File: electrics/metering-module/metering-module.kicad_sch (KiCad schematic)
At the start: 39 parts, among them J1 North, J2 South, J3 West, J4 East, Q1 MMBT3904, Q2 MMBT3904, U1 LTV-817S, U2 LTV-817S, U3 BA033CC0FP-E2, U4 MAX3486, U5 MAX3486, U6 MCP23009-E_SS

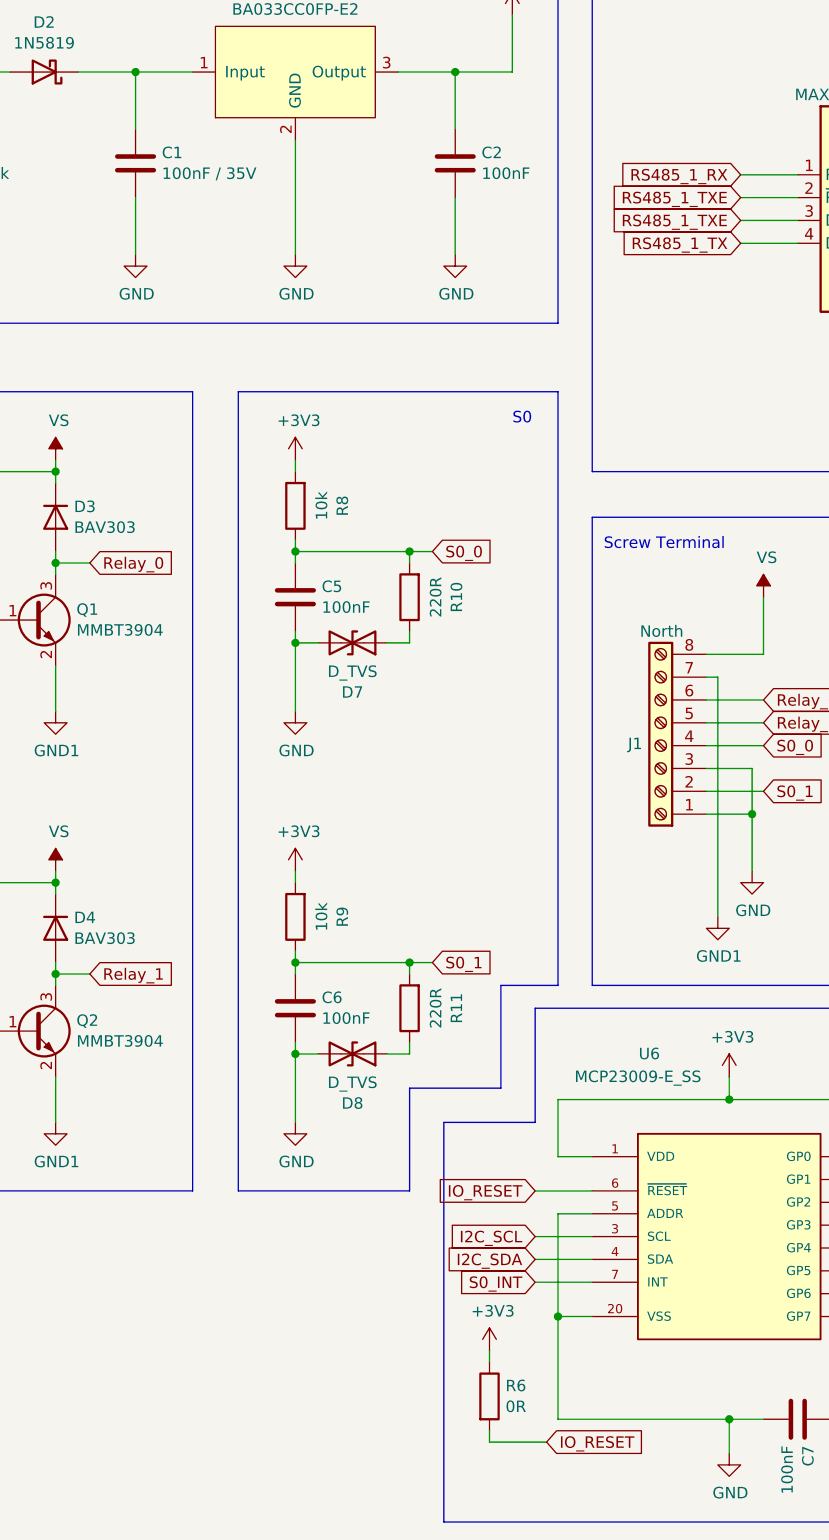
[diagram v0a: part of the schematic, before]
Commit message: Added product numbers for cost calculation
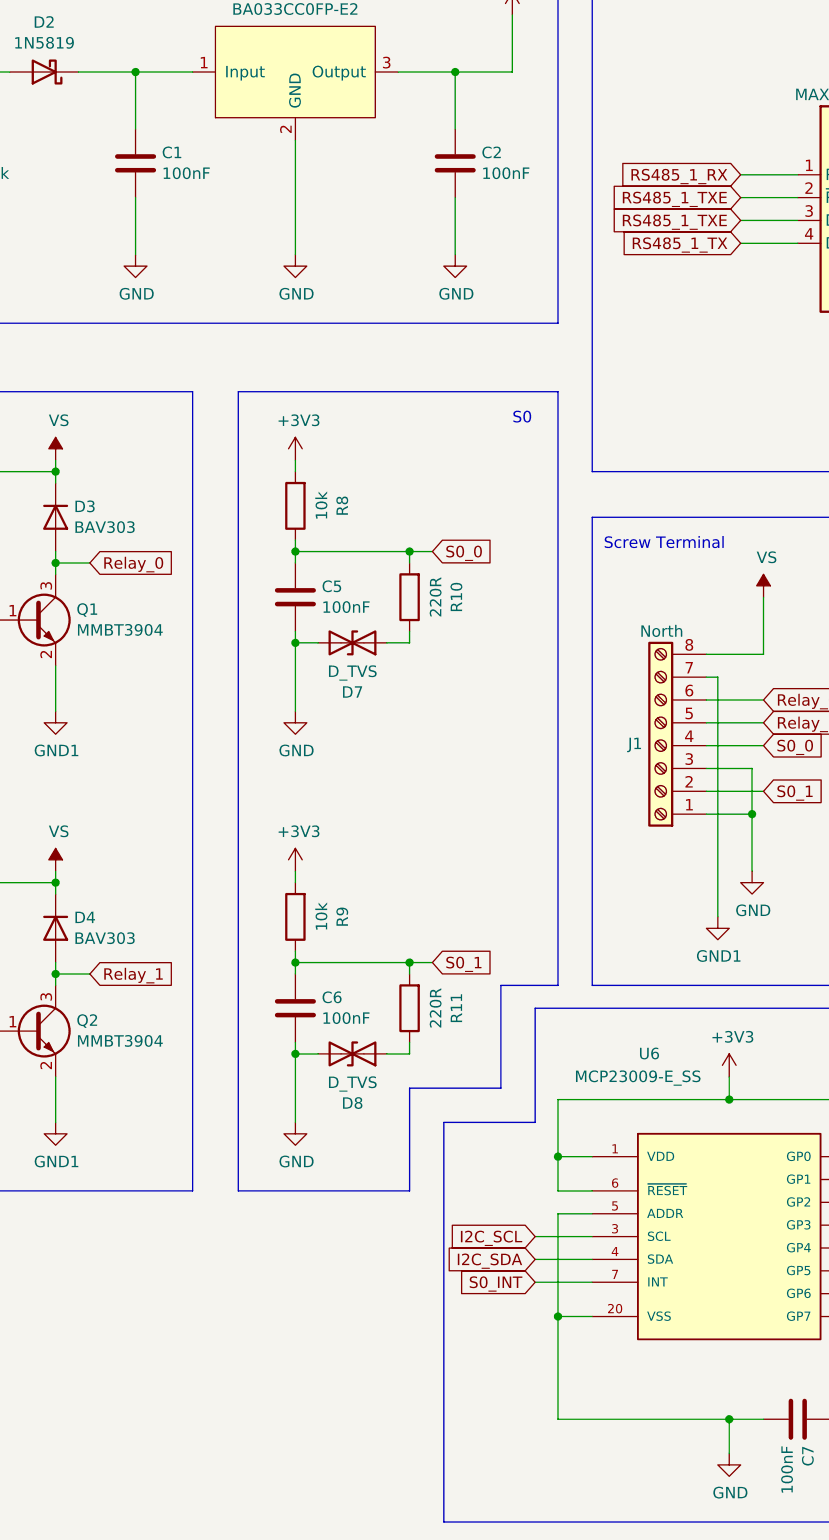
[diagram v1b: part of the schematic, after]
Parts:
- removed R6: 0R, Resistor_SMD:R_1206_3216Metric_Pad1.30x1.75mm_HandSolder, symbol Device:R
- C1: value 100nF / 35V -> 100nF
- D2: manf# (none) -> PMEG4010CEAX; mouser# (none) -> 771-PMEG4010CEAX
- D3, D4: manf# (none) -> BAV303-TR3; mouser# (none) -> 78-BAV303-TR3
- D7, D8: manf# (none) -> CG0603MLC-3.3LE; mouser# (none) -> 652-CG0603MLC-3.3LE
- F1: manf# (none) -> TR/3216FF1-R; mouser# (none) -> 504-TR/3216FF1-R
- G1, G2: now left out of the parts list
- J1, J2: manf# (none) -> 20020327-D081B01LF; mouser# (none) -> 649-220327-D081B01LF
- Q1, Q2: manf# (none) -> MMBT3904; mouser# (none) -> 771-MMBT3904T/R
- R1, R10, R11, R2: manf# (none) -> CR0603-FX-2200ELF; mouser# (none) -> 652-CR0603FX-2200ELF
- R3, R4: manf# (none) -> CR1206-FX-1001ELF; mouser# (none) -> 652-CR1206FX-1001ELF
- R5, R8, R9: manf# (none) -> CR1206-JW-103ELF; mouser# (none) -> 652-CR1206JW-103ELF
- U1, U2: manf# (none) -> LTV-817S; mouser# (none) -> 859-LTV-817S
- U3: manf# (none) -> BA033CC0FP-E2; mouser# (none) -> 755-BA033CC0FP-E2
- U4, U5: manf# (none) -> MAX3486EESA+; mouser# (none) -> 700-MAX3486EESA
- U6: manf# (none) -> MCP23009-E/SS; mouser# (none) -> 579-MCP23009-E/SS
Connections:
- net IO_RESET is gone; now on net +3V3: U6.6 (~{RESET})

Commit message: Feature/dedicated mieterstrom module (#9)
* Remove outdated files to clean things up

* Added missing part numbers for metering module

* Added 6 position screw terminal

* Added "mieterstrom" module

* Throw generated XML files out of version control

* Add "mieterstrom" module to local build

* Add "Mieterstrom" module to documentation

* Added "Mieterstrom" module to CI/CD
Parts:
- C1, C2, C3, C4, C5, C6, C7: manf# (none) -> C1206C104M6RACTU; mouser# (none) -> 80-C1206C104M6R
- D1: manf# (none) -> CPDU24V; mouser# (none) -> 750-CPDU24V
- J3, J4: manf# (none) -> M20-9991446; mouser# (none) -> 651-1935200
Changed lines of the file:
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@@
+      (effects (font (size 1.27 1.27)) hide)
+    )
+    (property "manf#" "C1206C104M6RACTU" (id 6) (at 80.01 44.45 0)
+      (effects (font (size 1.27 1.27)) hide)
+    )
+    (property "mouser#" "80-C1206C104M6R" (id 7) (at 80.01 44.45 0)
       (effects (font (size 1.27 1.27)) hide)
     )
@@
     )
     (property "Product" "https://www.mouser.de/ProductDetail/KEMET/C1206C104M6RACTU?qs=F5EMLAvA7IBTviv6fCZN3A%3D%3D" (id 5) (at 115.57 44.45 0)
+      (effects (font (size 1.27 1.27)) hide)
+    )
+    (property "manf#" "C1206C104M6RACTU" (id 6) (at 115.57 44.45 0)
+      (effects (font (size 1.27 1.27)) hide)
+    )
+    (property "mouser#" "80-C1206C104M6R" (id 7) (at 115.57 44.45 0)
       (effects (font (size 1.27 1.27)) hide)
     )
@@
     )
     (property "Product" "https://www.mouser.de/ProductDetail/KEMET/C1206C104M6RACTU?qs=F5EMLAvA7IBTviv6fCZN3A%3D%3D" (id 5) (at 180.34 39.37 0)
+      (effects (font (size 1.27 1.27)) hide)
+    )
+    (property "manf#" "C1206C104M6RACTU" (id 6) (at 180.34 39.37 0)
+      (effects (font (size 1.27 1.27)) hide)
+    )
+    (property "mouser#" "80-C1206C104M6R" (id 7) (at 180.34 39.37 0)
       (effects (font (size 1.27 1.27)) hide)
     )
@@
       (effects (font (size 1.27 1.27)) hide)
     )
+    (property "manf#" "C1206C104M6RACTU" (id 6) (at 256.54 39.37 0)
+      (effects (font (size 1.27 1.27)) hide)
+    )
+    (property "mouser#" "80-C1206C104M6R" (id 7) (at 256.54 39.37 0)
+      (effects (font (size 1.27 1.27)) hide)
+    )
     (pin "1")
     (pin "2")
@@
     )
     (property "Product" "https://www.mouser.de/ProductDetail/Harwin/M20-9991446" (id 5) (at 222.25 111.76 0)
+      (effects (font (size 1.27 1.27)) hide)
+    )
+    (property "manf#" "M20-9991446" (id 6) (at 222.25 111.76 0)
+      (effects (font (size 1.27 1.27)) hide)
+    )
+    (property "mouser#" "651-1935200" (id 7) (at 222.25 111.76 0)
       (effects (font (size 1.27 1.27)) hide)
     )
@@
       (effects (font (size 1.27 1.27)) hide)
     )
+    (property "manf#" "M20-9991446" (id 6) (at 260.35 111.76 0)
+      (effects (font (size 1.27 1.27)) hide)
+    )
+    (property "mouser#" "651-1935200" (id 7) (at 260.35 111.76 0)
+      (effects (font (size 1.27 1.27)) hide)
+    )
     (pin "1")
     (pin "10")
@@
       (effects (font (size 1.27 1.27)) hide)
     )
+    (property "manf#" "C1206C104M6RACTU" (id 6) (at 97.79 92.71 0)
+      (effects (font (size 1.27 1.27)) hide)
+    )
+    (property "mouser#" "80-C1206C104M6R" (id 7) (at 97.79 92.71 0)
+      (effects (font (size 1.27 1.27)) hide)
+    )
     (pin "1")
     (pin "2")
@@
       (effects (font (size 1.27 1.27)) hide)
     )
+    (property "manf#" "C1206C104M6RACTU" (id 6) (at 97.79 138.43 0)
+      (effects (font (size 1.27 1.27)) hide)
+    )
+    (property "mouser#" "80-C1206C104M6R" (id 7) (at 97.79 138.43 0)
+      (effects (font (size 1.27 1.27)) hide)
+    )
     (pin "1")
     (pin "2")
@@
       (effects (font (size 1.27 1.27)) hide)
     )
+    (property "manf#" "C1206C104M6RACTU" (id 6) (at 153.67 184.15 0)
+      (effects (font (size 1.27 1.27)) hide)
+    )
+    (property "mouser#" "80-C1206C104M6R" (id 7) (at 153.67 184.15 0)
+      (effects (font (size 1.27 1.27)) hide)
+    )
     (pin "1")
     (pin "2")
@@
       (effects (font (size 1.27 1.27)) hide)
     )
+    (property "manf#" "CPDU24V" (id 6) (at 48.26 44.45 0)
+      (effects (font (size 1.27 1.27)) hide)
+    )
+    (property "mouser#" "750-CPDU24V" (id 7) (at 48.26 44.45 0)
+      (effects (font (size 1.27 1.27)) hide)
+    )

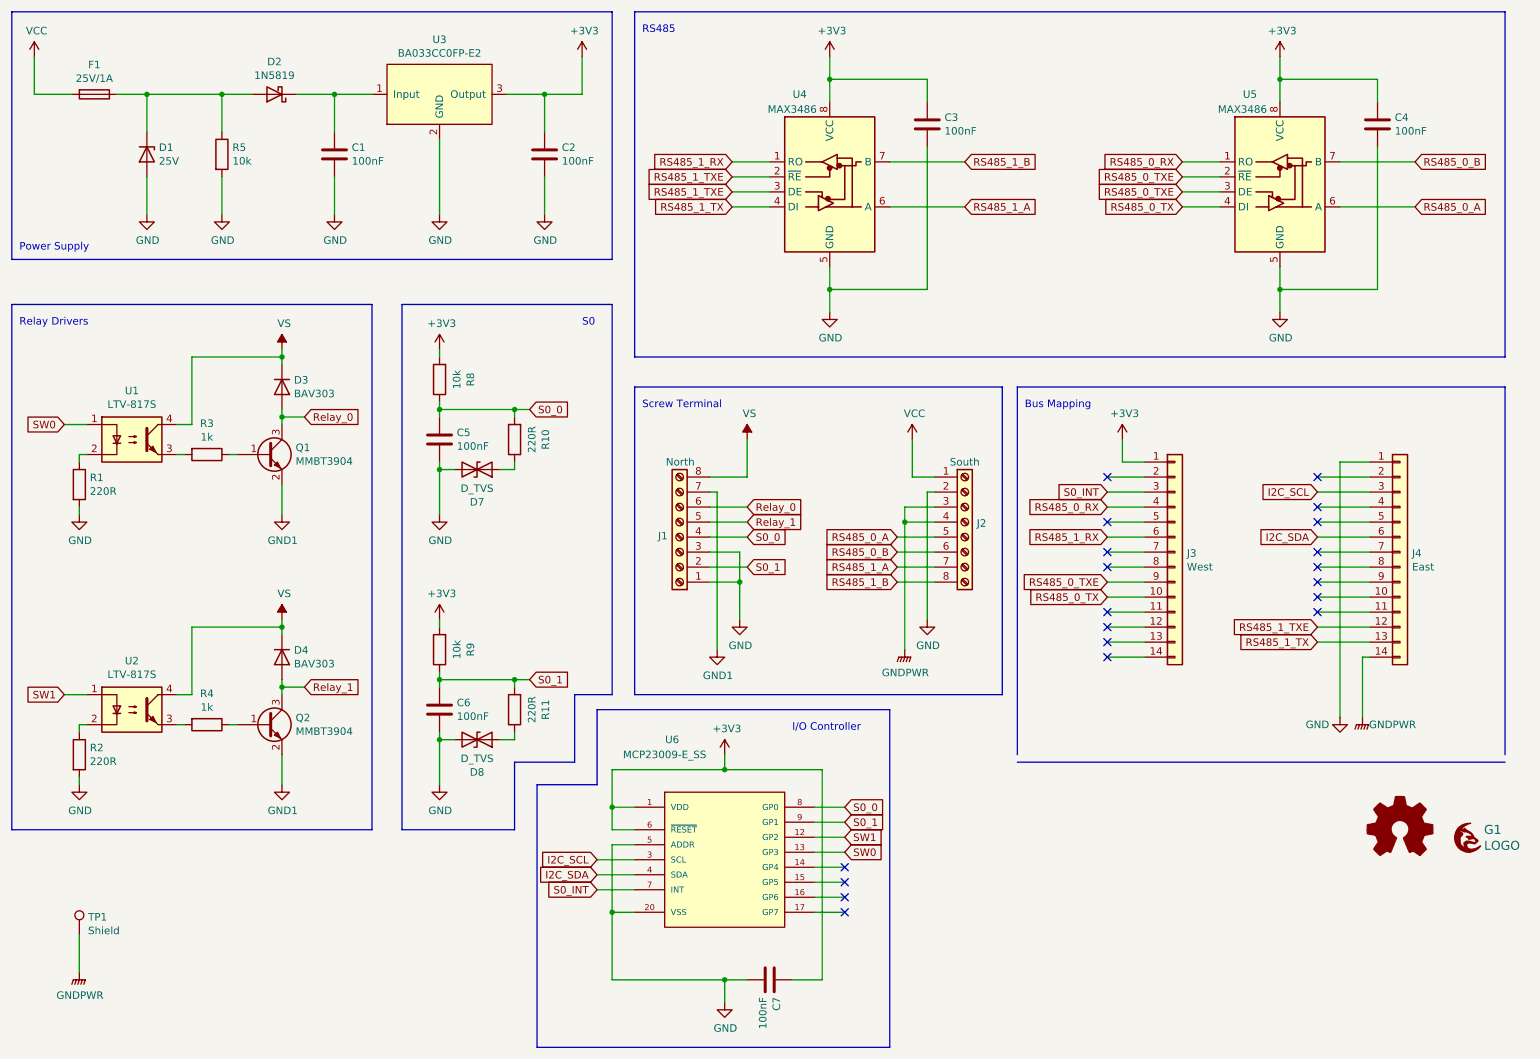
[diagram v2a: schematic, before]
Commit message: Fix all ERC and DRC warnings during build
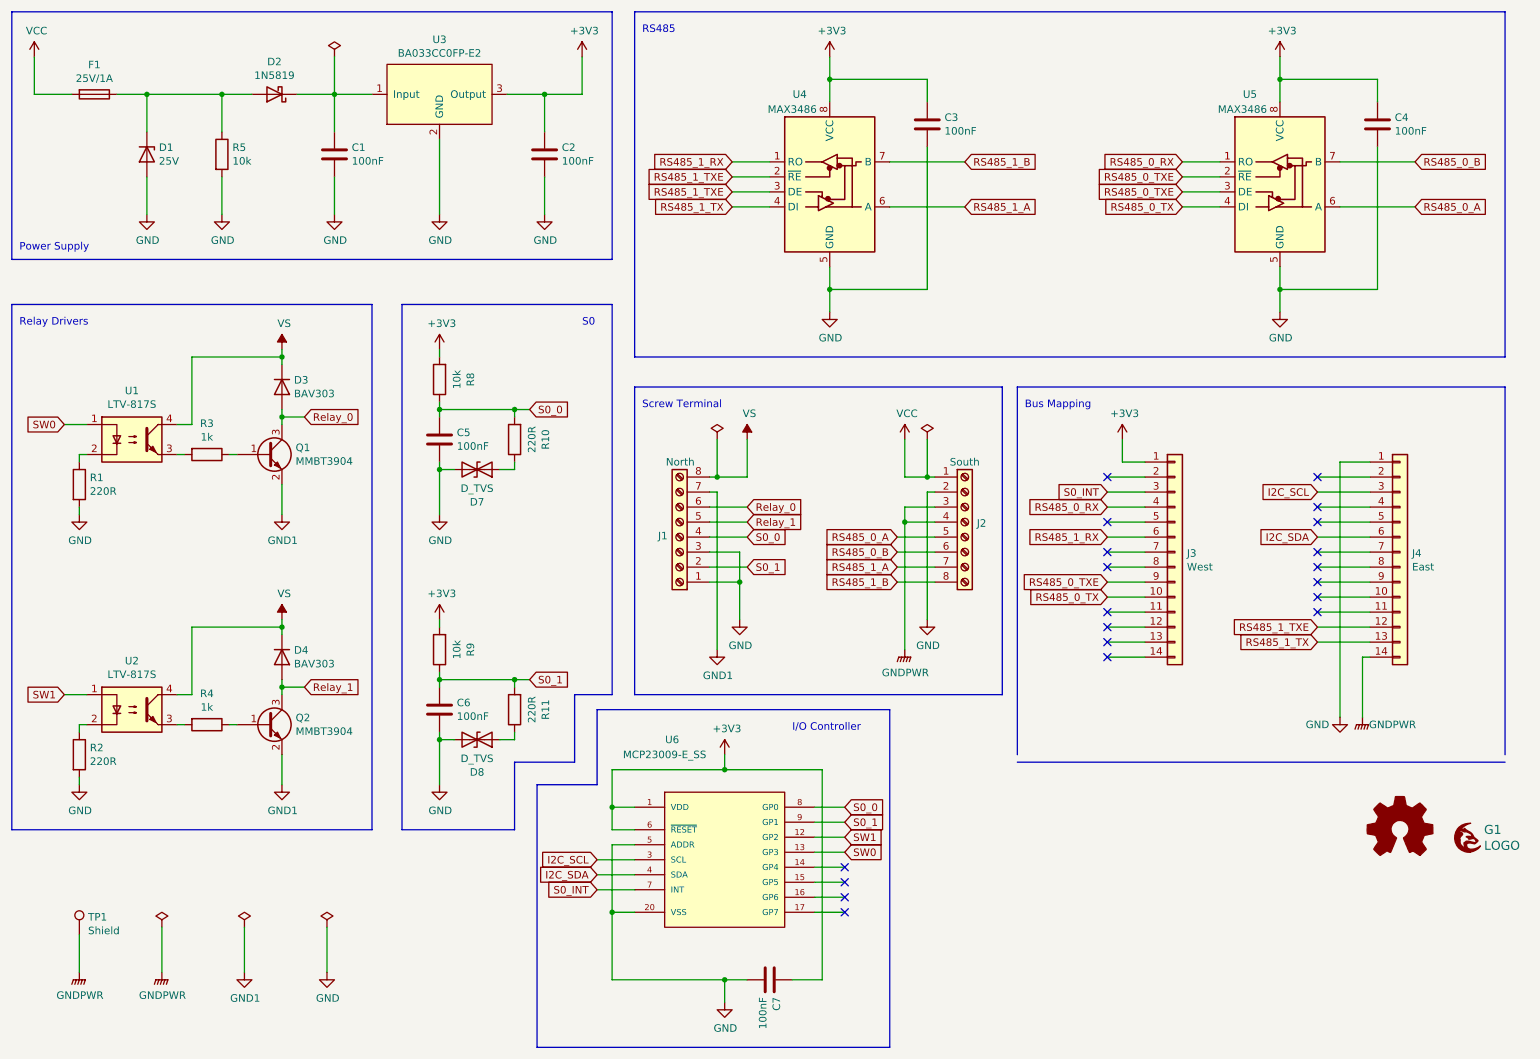
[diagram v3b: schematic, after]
